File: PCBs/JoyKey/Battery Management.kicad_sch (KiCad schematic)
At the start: 14 parts, among them J4 JST PH, Q1 DMG3415, U1 AP2112K-3.3, U8 MCP73831-2-OT

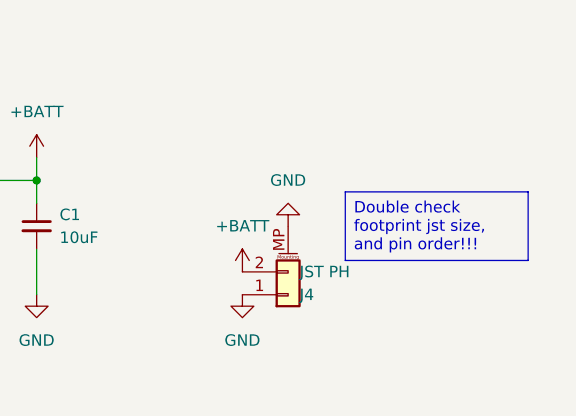
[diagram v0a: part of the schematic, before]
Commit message: Reverse polarity of JST to match Adafruit Battery polarity
It was an issue I had missed in my review
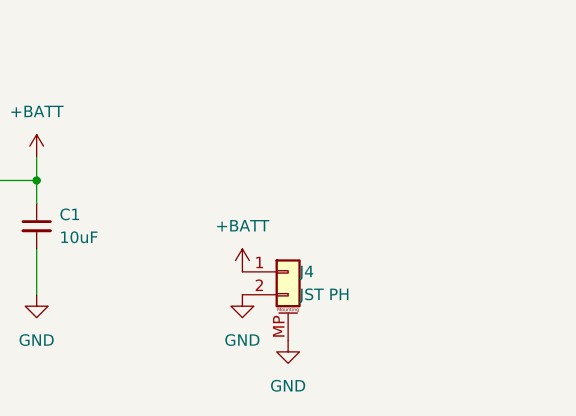
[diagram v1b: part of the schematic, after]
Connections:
- net +BATT: now also J4.1 (Pin_1); no longer J4.2 (Pin_2)
- net GND: now also J4.2 (Pin_2); no longer J4.1 (Pin_1)
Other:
- moved on the sheet: J4
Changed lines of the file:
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@@
-		)
-	)
-	(text_box "Double check footprint jst size, and pin order!!!"
-		(exclude_from_sim no)
-		(at 260.35 110.49 0)
-		(size 20.32 7.62)
-		(margins 0.9525 0.9525 0.9525 0.9525)
-		(stroke
-			(width 0)
-			(type default)
-			(color 255 0 0 1)
-		)
-		(fill
-			(type none)
-		)
-		(effects
-			(font
-				(size 1.27 1.27)
-				(color 255 0 0 1)
-			)
-			(justify left top)
 		)
 	)
@@
 	(symbol
 		(lib_id "power:GND")
-		(at 254 114.3 180)
+		(at 254 127 0)
+		(mirror y)
 		(unit 1)
 		(exclude_from_sim no)
@@
 		(fields_autoplaced yes)
 		(property "Reference" "#PWR26"
-			(at 254 107.95 0)
+			(at 254 133.35 0)
 			(effects
 				(font
@@
 		)
 		(property "Value" "GND"
-			(at 254 109.22 0)
+			(at 254 132.08 0)
 			(effects
 				(font
@@
 		)
 		(property "Footprint" ""
-			(at 254 114.3 0)
+			(at 254 127 0)
 			(effects
 				(font
@@
 		)
 		(property "Datasheet" ""
-			(at 254 114.3 0)
+			(at 254 127 0)
 			(effects
 				(font
@@
 		)
 		(property "Description" "Power symbol creates a global label with name \"GND\" , ground"
-			(at 254 114.3 0)
+			(at 254 127 0)
 			(effects
 				(font
@@
 	(symbol
 		(lib_id "Connector_Generic_MountingPin:Conn_01x02_MountingPin")
-		(at 254 121.92 0)
-		(mirror x)
+		(at 254 119.38 0)
 		(unit 1)
 		(exclude_from_sim no)
@@
 		(dnp no)
 		(property "Reference" "J4"
-			(at 255.27 121.9201 0)
+			(at 255.27 119.3799 0)
 			(effects
 				(font
@@
 		)
 		(property "Value" "JST PH"
-			(at 255.27 119.3801 0)
+			(at 255.27 121.9199 0)
 			(effects
 				(font
@@
 		)
 		(property "Footprint" "Connector_JST:JST_PH_S2B-PH-SM4-TB_1x02-1MP_P2.00mm_Horizontal"
-			(at 254 121.92 0)
+			(at 254 119.38 0)
 			(effects
 				(font
@@
 		)
 		(property "Datasheet" "~"
-			(at 254 121.92 0)
+			(at 254 119.38 0)
 			(effects
 				(font
@@
 		)
 		(property "Description" "Generic connectable mounting pin connector, single row, 01x02, script generated (kicad-library-utils/schlib/autogen/connector/)"
-			(at 254 121.92 0)
-			(effects
-				(font
+			(at 254 119.38 0)
+			(effects
+				(font

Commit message: Updated BOM with LCSC parts
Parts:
- C1, C3, C4, C5: LCSC (none) -> C15850
- D20: LCSC (none) -> C2286
- D24: LCSC (none) -> C78545
- J4: LCSC (none) -> C295747
- Q1: LCSC (none) -> C7202986
- R1, R3, R4: LCSC (none) -> C17414
- R2: LCSC (none) -> C17604
- U1: LCSC (none) -> C51118
- U8: LCSC (none) -> C424093
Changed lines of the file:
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@@
+			)
+		)
+		(property "LCSC" "C78545"
+			(at 120.65 109.22 0)
+			(effects
+				(font
+					(size 1.27 1.27)
+				)
+				(hide yes)
 			)
 		)
@@
 			)
 		)
+		(property "LCSC" "C7202986"
+			(at 72.39 104.14 0)
+			(effects
+				(font
+					(size 1.27 1.27)
+				)
+				(hide yes)
+			)
+		)
 		(pin "3"
 		)
@@
 			)
 		)
+		(property "LCSC" "C2286"
+			(at 210.82 114.3 0)
+			(effects
+				(font
+					(size 1.27 1.27)
+				)
+				(hide yes)
+			)
+		)
 		(pin "1"
 		)
@@
 			)
 		)
+		(property "LCSC" "C295747"
+			(at 254 119.38 0)
+			(effects
+				(font
+					(size 1.27 1.27)
+				)
+				(hide yes)
+			)
+		)
 		(pin "1"
 		)
@@
 			)
 		)
+		(property "LCSC" "C15850"
+			(at 114.3 111.76 0)
+			(effects
+				(font
+					(size 1.27 1.27)
+				)
+				(hide yes)
+			)
+		)
 		(pin "1"
 		)
@@
 			)
 		)
+		(property "LCSC" "C17414"
+			(at 83.82 113.03 0)
+			(effects
+				(font
+					(size 1.27 1.27)
+				)
+				(hide yes)
+			)
+		)
 		(pin "2"
 		)
@@
 			)
 		)
+		(property "LCSC" "C424093"
+			(at 182.88 111.76 0)
+			(effects
+				(font
+					(size 1.27 1.27)
+				)
+				(hide yes)
+			)
+		)
 		(pin "2"
 		)
@@
 			)
 		)
+		(property "LCSC" "C17414"
+			(at 199.39 114.3 90)
+			(effects
+				(font
+					(size 1.27 1.27)
+				)
+				(hide yes)
+			)
+		)
 		(pin "2"
 		)
@@
 			)
 		)
+		(property "LCSC" "C15850"
+			(at 74.93 116.84 0)
+			(effects
+				(font
+					(size 1.27 1.27)
+				)
+				(hide yes)
+			)
+		)
 		(pin "1"
 		)
@@
 			)
 		)
+		(property "LCSC" "C15850"
+			(at 226.06 114.3 0)
+			(effects
+				(font
+					(size 1.27 1.27)
+				)
+				(hide yes)
+			)
+		)
 		(pin "1"
 		)
@@
 			)
 		)
+		(property "LCSC" "C15850"
+			(at 127 111.76 0)
+			(effects
+				(font
+					(size 1.27 1.27)
+				)
+				(hide yes)
+			)
+		)
 		(pin "1"
 		)
@@
 			)
 		)
+		(property "LCSC" "C17604"
+			(at 170.18 118.11 0)
+			(effects
+				(font
+					(size 1.27 1.27)
+				)
+				(hide yes)
+			)
+		)
 		(pin "2"
 		)
@@
 			)
 		)
+		(property "LCSC" "C51118"
+			(at 102.87 111.76 0)
+			(effects
+				(font
+					(size 1.27 1.27)
+				)
+				(hide yes)
+			)
+		)
 		(pin "1"
 		)
@@
 			(at 59.69 113.03 0)
 			(effects
+				(font
+					(size 1.27 1.27)
+				)
+				(hide yes)
+			)
+		)
+		(property "LCSC" "C17414"
+			(at 59.69 113.03 0)
+			(effects
